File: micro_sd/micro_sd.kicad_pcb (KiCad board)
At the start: 4 copper layers, 10 parts

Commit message: [Rushil] small change in pcb
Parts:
- C1, C2: footprint Capacitor_SMD:C_0603_1608Metric -> Library:C_0603_1608Metric
- MICRO_SD1: footprint TF-01A:TF-01A -> Library:TF-01A
- R1, R2, R3, R4, R5, R6, R7: footprint Resistor_SMD:R_0603_1608Metric -> Library:R_0603_1608Metric
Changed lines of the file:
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@@
 	(net 8 "/block_micro_sd/DAT1")
 	(net 9 "/block_micro_sd/DET_A")
-	(footprint "Resistor_SMD:R_0603_1608Metric"
+	(footprint "Library:R_0603_1608Metric"
 		(layer "F.Cu")
 		(at 137.89 80.585 -90)
@@
 		)
 	)
-	(footprint "Resistor_SMD:R_0603_1608Metric"
+	(footprint "Library:R_0603_1608Metric"
 		(layer "F.Cu")
 		(at 147.71 80.585 -90)
@@
 		)
 	)
-	(footprint "Resistor_SMD:R_0603_1608Metric"
+	(footprint "Library:R_0603_1608Metric"
 		(layer "F.Cu")
 		(at 142.71 80.585 -90)
@@
 		)
 	)
-	(footprint "TF-01A:TF-01A"
+	(footprint "Library:TF-01A"
 		(layer "F.Cu")
 		(at 146.0638 92.75)
@@
 		)
 	)
-	(footprint "Capacitor_SMD:C_0603_1608Metric"
+	(footprint "Library:C_0603_1608Metric"
 		(layer "F.Cu")
 		(at 144.34 80.585 90)
@@
 		)
 	)
-	(footprint "Resistor_SMD:R_0603_1608Metric"
+	(footprint "Library:R_0603_1608Metric"
 		(layer "F.Cu")
 		(at 151.19 80.585 -90)
@@
 		)
 	)
-	(footprint "Resistor_SMD:R_0603_1608Metric"
+	(footprint "Library:R_0603_1608Metric"
 		(layer "F.Cu")
 		(at 149.58 80.585 -90)
@@
 		)
 	)
-	(footprint "Resistor_SMD:R_0603_1608Metric"
+	(footprint "Library:R_0603_1608Metric"
 		(layer "F.Cu")
 		(at 141.1 80.585 -90)
@@
 		)
 	)
-	(footprint "Resistor_SMD:R_0603_1608Metric"
+	(footprint "Library:R_0603_1608Metric"
 		(layer "F.Cu")
 		(at 139.49 80.585 -90)
@@
 		)
 	)
-	(footprint "Capacitor_SMD:C_0603_1608Metric"
+	(footprint "Library:C_0603_1608Metric"
 		(layer "F.Cu")
 		(at 145.91 80.585 90)

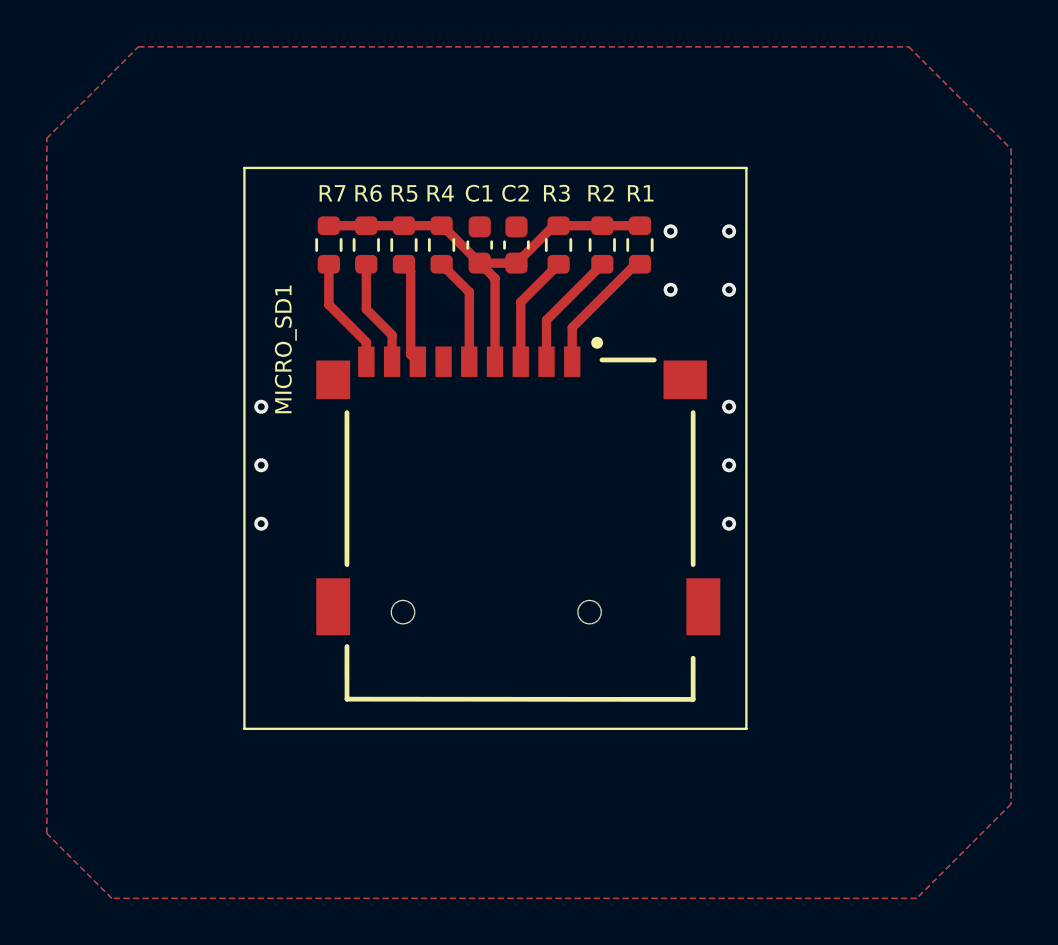
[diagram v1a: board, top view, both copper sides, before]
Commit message: fixed microsd
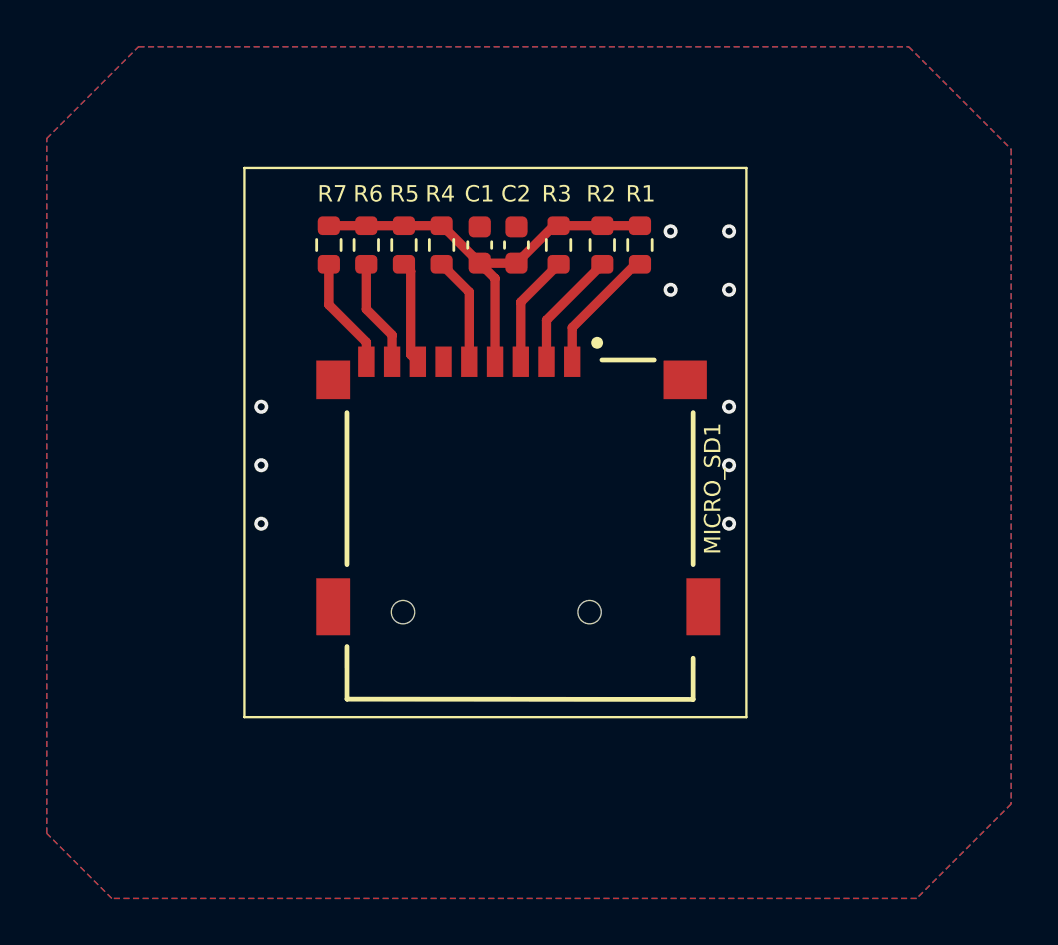
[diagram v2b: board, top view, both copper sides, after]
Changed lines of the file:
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@@
 			(psa4output no)
 			(plot_black_and_white yes)
+			(plotinvisibletext no)
 			(sketchpadsonfab no)
 			(plotpadnumbers no)
@@
 		(descr "<b>TF-01A-6</b><br>")
 		(property "Reference" "MICRO_SD1"
-			(at -10.0938 -7.7 90)
+			(at 8.2362 -1.75 90)
 			(layer "F.SilkS")
 			(effects
@@
 	(gr_rect
 		(start 134.28 77.29)
-		(end 155.74 101.27)
+		(end 155.74 100.77)
 		(stroke
 			(width 0.1)
@@
 	(gr_rect
 		(start 134.28 77.29)
-		(end 155.74 101.27)
+		(end 155.74 100.77)
 		(stroke
 			(width 0.1)
